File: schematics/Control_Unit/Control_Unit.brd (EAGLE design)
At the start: 49.8 x 49.8 mm, 238 parts, among them IC1 74HCT32N, IC10 74HC74N, IC100 74HCT374N, IC101 74HCT08N, IC102 74HC151N, IC103 74HC373N, IC105 74HC151N, IC106 74HC151N, IC108 74HCT32N, IC11 74HC74N, IC110 74HCT32N, IC111 74HC151N, IC112 74HCT32N, IC113 74HC151N, IC114 74HC151N, IC115 74HC151N, IC116 74HC373N, IC117 74HC74N, IC12 74AC08N, IC124 74HCT32N, IC125 74HCT08N, IC126 74AC157N, IC127 74HCT08N, IC128 74AC08N, IC129 74AC08N, IC13 74AC08N, IC135 74HCT08N, IC136 74HCT08N, IC14 74HC74N, IC141 74HCT32N, IC15 74HC74N, IC16 74AC08N, IC168 74HCT32N, IC169 74HCT32N, IC17 74HCT32N, IC172 74HCT32N, IC173 74HCT32N, IC175 74HC193N, IC176 74HC193N, IC177 74HC193N, IC178 74HC193N, IC179 74HC193N, IC18 74AC08N, IC180 74HC193N, IC181 74HC193N, IC182 74HC193N, IC19 74AC08N, IC190 74HCT32N, IC191 74HCT32N, IC20 74AC08N, IC21 74AC08N, IC22 74HCT32N, IC23 74HCT08N, IC24 74HCT08N, IC26 74HCT08N, IC27 74HCT08N, IC28 74HCT08N, IC29 74HCT32N, IC3 74HC151N, IC30 74HCT08N, IC31 74HCT00N, IC33 74HCT32N, IC34 74HCT08N, IC35 74HCT04N, IC36 74HCT32N, IC38 74HCT08N, IC39 74HCT08N, IC4 74AC08N, IC41 74HCT08N, IC42 74HC373N, IC43 74HCT04N, IC44 74ACT157N, IC46 74ACT157N, IC47 74HCT04N, IC48 74ACT02N, IC49 74AC86N, IC5 74ACT02N, IC51 74HCT08N, IC52 74HCT32N, IC55 74HCT32N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

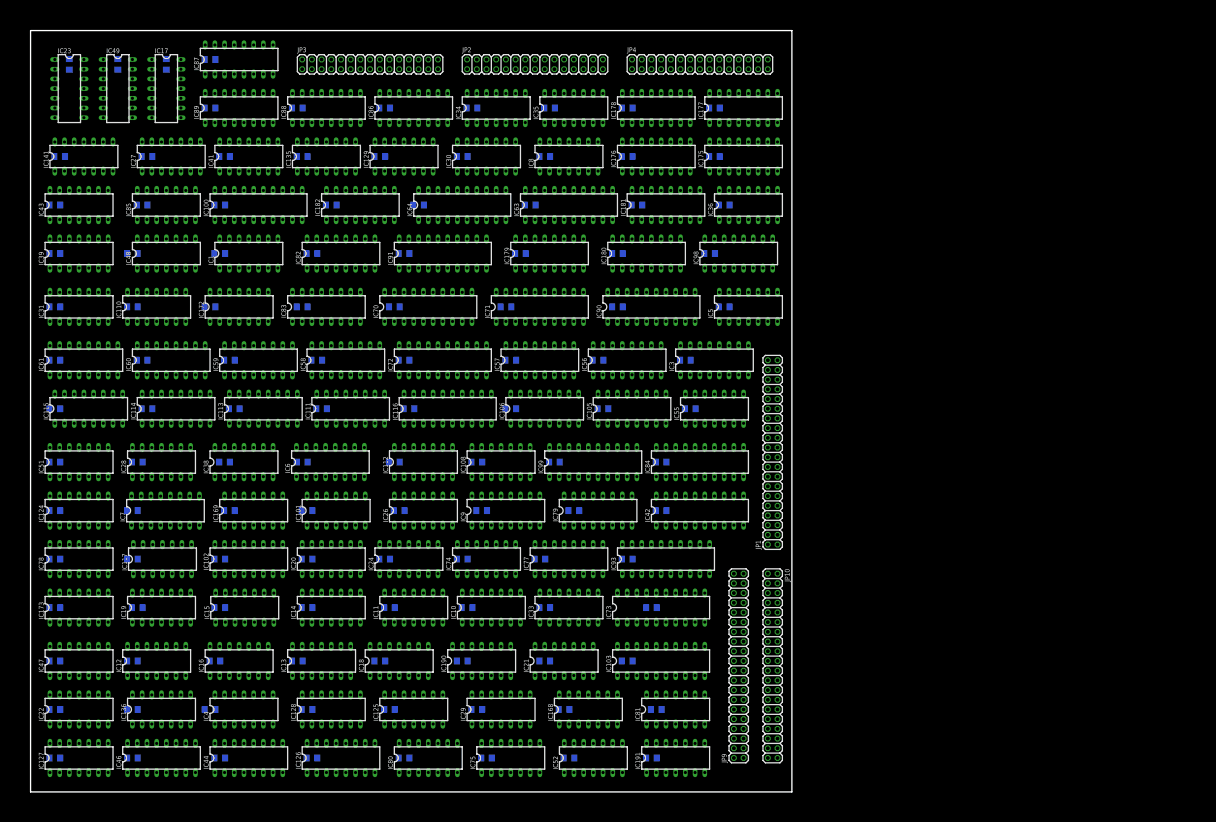
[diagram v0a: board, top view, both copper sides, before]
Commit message: got rid of two cycles! finetuning next
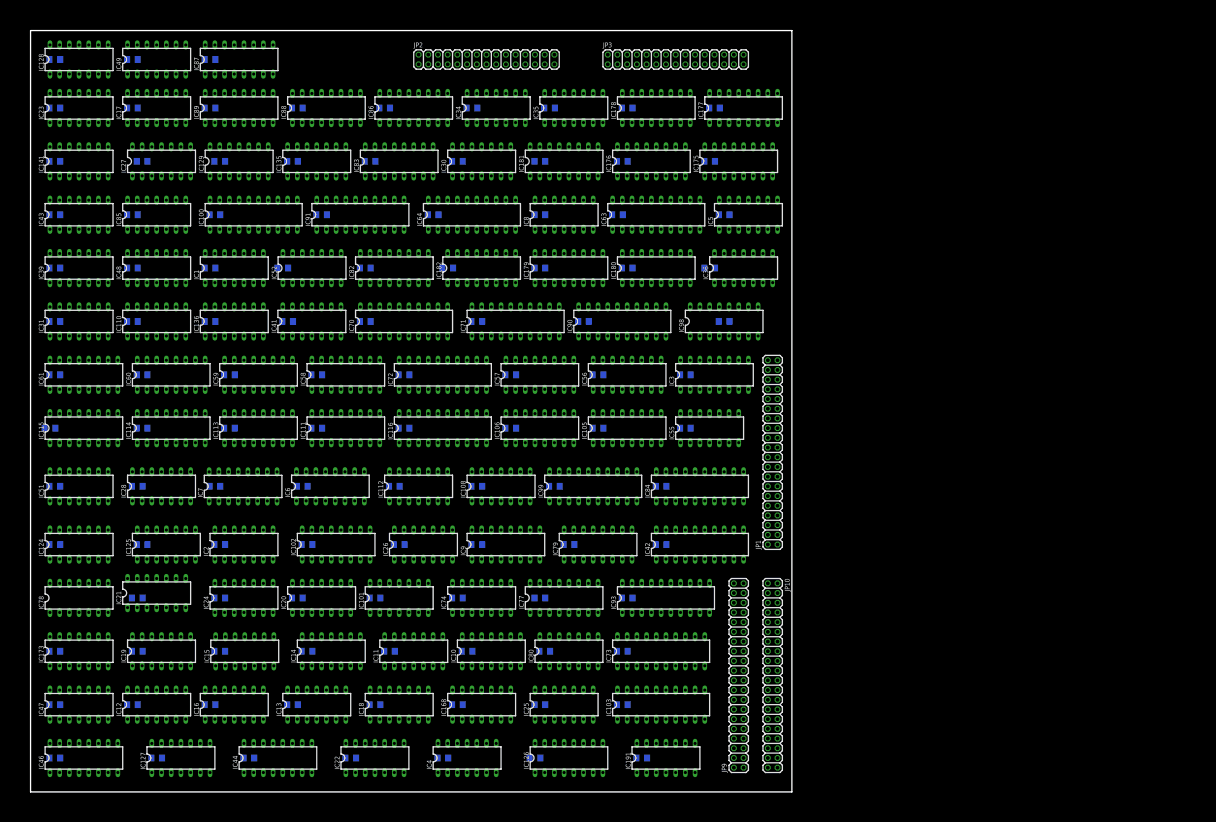
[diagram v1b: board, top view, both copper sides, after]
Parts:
- removed C100, C101, C124, C149, C155, C37, C54, C62: (no value), rcl:C1206
- removed IC117: 74HC74N, 74xx-eu:DIL14
- removed IC169, IC172, IC190, IC29, IC33: 74HCT32N, 74xx-eu:DIL14
- removed IC38, IC75, IC81: 74HCT08N, 74xx-eu:DIL14
- removed JP4: (no value), pinhead:2X15
- added IC2, IC25: 74HCT32N, 74xx-eu:DIL14
- moved C5 48.5 mm to (44.5, 41.3)
- moved C4 48.1 mm to (38.7, 41.3)
- moved IC128 45.6 mm to (3.17, 47.9)
- moved C2 39.4 mm to (1.59, 44.8)
- moved IC52 37.0 mm to (18.4, 34.3)
- moved C74 34.5 mm to (11.7, 34.3)
- moved C145 32.4 mm to (19.1, 37.8)
- moved IC21 27.0 mm to (8.26, 13.0)
- moved IC136 25.8 mm to (13.3, 30.8)
- moved C59 20.1 mm to (42.9, 23.8)
- moved JP3 20.0 mm to (42.2, 47.9)
- moved IC22 19.6 mm to (22.5, 2.22)
- moved IC125 19.5 mm to (8.89, 16.2)
- moved IC4 14.9 mm to (28.6, 2.22)
- moved IC126 14.9 mm to (35.2, 2.22)
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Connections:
- removed net CLR_NOT_CS_LDR: IC17.4, IC173.1, IC173.6
- removed net CLR_NOT_CS_POP: IC172.8, IC48.11, IC85.9
- removed net CONNECT_REG_TO_DBUS_PTR: IC172.11, IC52.4
- removed net FILL_LR_H_SAVE_LR: IC29.9, IC5.11, IC81.3
- removed net FILL_LR_L_SAVE_LR: IC29.1, IC5.8, IC81.8
- removed net FILL_PC_H_RET: IC1.4, IC29.12, IC51.11
- removed net FILL_PC_L_JMP_O: IC1.12, IC101.10, IC33.1, IC38.11
- removed net FILL_PC_L_RET: IC1.13, IC29.4, IC51.3
- removed net FILL_PTR_H_SET_PTR: IC169.1, IC26.8, IC5.3
- removed net FILL_PTR_L_PTR_ADD: IC24.8, IC31.13, IC33.2
- removed net FILL_PTR_L_SET_PTR: IC169.10, IC172.12, IC26.3
- removed net FILL_REGISTER_ALU/ALU_TO_DBUS: IC117.11, IC169.13, IC169.4, IC75.11
- removed net FILL_REGISTER_LDR: IC108.5, IC173.4, IC27.6
- removed net FILL_REGISTER_MOV: IC169.12, IC190.4, IC74.6
- removed net FILL_REGISTER_POP: IC108.4, IC172.9, IC24.6
- removed net IR_LOAD_INPUT: IC127.3, IC80.12, IC90.11
- removed net N$112: IC29.2, IC81.11
- removed net N$122: IC173.5, IC27.3
- removed net N$143: IC168.11, IC168.4
- removed net N$147: IC169.5, IC33.3
- removed net N$155: IC168.12, IC168.3
- removed net N$156: IC172.10, IC24.3
- removed net N$160: IC169.2, IC26.6
- removed net N$18: IC169.6, IC43.9
- removed net N$196: IC172.13, IC24.11
- removed net N$204: IC190.2, IC74.8
- removed net N$223: IC29.5, IC51.6
- removed net N$226: IC29.13, IC51.8
- removed net N$233: IC29.10, IC81.6
- removed net N$56: IC190.5, IC74.3
- removed net PC_COUNT_UP_FETCH2/CYCL_5: IC1.2, IC14.12, IC14.5, JP1.30
- removed net PC_HIGH_LOAD_INPUT_JMP: IC190.9, IC28.11, IC48.5
- removed net PC_LOW_LOAD_INPUT_JMP: IC1.9, IC190.1, IC74.11
- removed net STATE_0/CYCL_6: IC125.1, IC14.9, IC15.2, IC23.12, IC24.12, IC27.9, IC28.1, IC31.9, IC38.9, IC51.4, IC74.1, IC74.9, IC78.12, IC81.12, JP1.32
- removed net STATE_1/CYCL_7: IC15.12, IC15.5, IC23.1, IC23.4, IC24.1, IC26.1, IC27.1, IC27.12, IC38.1, IC51.1, IC74.12, IC74.4, IC75.1, IC81.9, JP1.34
- removed net STATE_2/CYCL_8: IC117.2, IC15.9, IC23.9, IC24.4, IC26.4, IC27.4, IC28.4, IC28.9, IC38.4, IC51.9, IC75.4, IC81.4, JP1.36
- removed net STATE_3/CYCL_9: IC10.2, IC117.5, IC24.9, IC26.9, IC28.12, IC31.1, IC38.12, IC51.12, IC75.12, IC81.1, JP1.38
- removed net WRITE_LR_H_DBUS_RET: IC141.2, IC29.11, IC36.4
- removed net WRITE_LR_L_DBUS_RET: IC141.1, IC29.6
- removed net WRITE_PC_H_DBUS_SAVE_LR: IC141.13, IC29.8
- removed net WRITE_PC_L_DBUS_SAVE_LR: IC141.12, IC29.3, IC36.5
- removed net WRITE_REGB_TO_DBUS_ALU: IC168.9, IC75.6
- removed net WRITE_REGB_TO_DBUS_JMP: IC168.13, IC190.8
- removed net WRITE_REGB_TO_DBUS_JMP_O: IC168.2, IC38.6
- removed net WRITE_REGB_TO_DBUS_PTR_ADD: IC168.1, IC28.6
- removed net WRITE_REGB_TO_DBUS_SET_PTR: IC168.10, IC169.3
- removed net WRITE_REG_TO_DBUS_JMP: IC190.3, IC52.1
- removed net WRITE_REG_TO_DBUS_MOV: IC190.6, IC52.5
- new net CLR_NOT_CS_LDR/FILL_REGISTER_LDR: IC108.5, IC17.4, IC173.1, IC27.8
- new net CLR_NOT_CS_POP/FILL_REGISTER_POP: IC108.4, IC125.3, IC48.11, IC85.9
- new net CONNECT_REG_TO_DBUS_PTR/FILL_PTR_L_SET_PTR: IC24.11, IC48.3, IC52.4
- new net IR_LOAD_INPUT/PC_COUNT_UP_FETCH2: IC1.2, IC127.3, IC80.12, IC90.11
- new net PTR_ADD_OR_JMP_O_OR_ALU_FILL: IC168.4, IC168.8, IC43.9
- new net STATE_0/CYCL_5: IC14.12, IC14.5, IC24.1, IC24.12, IC24.4, IC24.9, IC31.9, IC51.12, IC51.4, IC51.9, IC74.1, IC74.12, IC74.4, IC74.9, JP1.30
- new net STATE_1/CYCL_6: IC125.1, IC14.9, IC15.2, IC23.1, IC26.1, IC26.4, IC27.12, IC27.4, IC27.9, IC28.1, IC28.9, IC51.1, IC78.12, JP1.32
- new net STATE_2/CYCL_7: IC10.2, IC15.5, IC23.4, IC27.1, IC28.12, IC28.4, IC31.1, JP1.34
- new net WRITE_LR_H_DBUS_RET/FILL_PC_H_RET: IC1.4, IC141.2, IC36.4, IC51.3
- new net WRITE_LR_L_DBUS_RET/FILL_PC_L_RET: IC1.13, IC141.1, IC24.3
- new net WRITE_PC_H_DBUS_SAVE_LR/FILL_LR_H_SAVE_LR: IC141.13, IC26.6, IC5.11
- new net WRITE_PC_L_DBUS_SAVE_LR/FILL_LR_L_SAVE_LR: IC141.12, IC24.8, IC36.5, IC5.8
- new net WRITE_REGB_TO_DBUS_ALU/FILL_REGISTER_ALU/ALU_TO_DBUS: IC15.11, IC168.10, IC2.13, IC23.6
- new net WRITE_REGB_TO_DBUS_JMP/PC_HIGH_LOAD_INPUT_JMP: IC168.12, IC28.8, IC5.5
- new net WRITE_REGB_TO_DBUS_JMP_O/FILL_PC_L_JMP_O: IC1.12, IC101.10, IC168.2, IC28.11
- new net WRITE_REGB_TO_DBUS_PTR_ADD/FILL_PTR_L_PTR_ADD: IC168.1, IC28.6, IC31.13
- new net WRITE_REGB_TO_DBUS_SET_PTR/FILL_PTR_H_SET_PTR: IC168.13, IC26.3, IC48.6
- new net WRITE_REG_TO_DBUS_JMP/PC_LOW_LOAD_INPUT_JMP: IC1.9, IC52.1, IC74.8
- new net WRITE_REG_TO_DBUS_MOV/FILL_REGISTER_MOV: IC2.12, IC52.5, IC74.3
- net !CLR_CARRY_BIT: now also IC15.13; no longer IC117.13
- net !OPCODE_5: now also IC26.10; no longer IC75.10
- net !RING_CNTR_RESET: no longer IC117.1, IC15.13
- net !SET_CARRY_BIT: now also IC15.10; no longer IC117.10
- net ADRR_0: no longer JP3.1
- net ADRR_1: no longer JP3.3
- net ADRR_10: no longer JP3.21
- net ADRR_11: no longer JP3.23
- net ADRR_12: no longer JP3.25
- net ADRR_13: no longer JP3.27
- net ADRR_14: no longer JP3.29
- net ADRR_2: no longer JP3.5
- net ADRR_3: no longer JP3.7
- net ADRR_4: no longer JP3.9
- net ADRR_5: no longer JP3.11
- net ADRR_6: no longer JP3.13
- net ADRR_7: no longer JP3.15
- net ADRR_8: no longer JP3.17
- net ADRR_9: no longer JP3.19
- net ALU_CARRY_BIT: now also IC15.9; no longer IC117.9
- net ALU_CARRY_OUT: now also IC15.12; no longer IC117.12
- net ALU_NR1_ENABLE_ALU: now also IC25.9; no longer IC33.9
- net ALU_NR1_ENABLE_JMP_O_PTR_ADD: now also IC25.10; no longer IC33.10
- net ALU_NR2_ENABLE_ALU: now also IC25.12; no longer IC33.4
- net ALU_NR2_ENABLE_JMP_O_PTR_ADD: now also IC25.13; no longer IC33.5
- net CLR_NOT_CS_PUSH: now also IC173.4, IC27.3; no longer IC172.1, IC23.8
- net CLR_NOT_OE/CLR_NOT_CS_CYCL_0: now also IC85.11; no longer IC48.8
- net CLR_NOT_OE_POP: now also JP3.4; no longer JP4.20
- net CONNECT_PTR_TO_ABUS/CLR_NOT_OE_LDR: now also IC85.12; no longer IC48.9
- net CONNECT_PTR_TO_ABUS/CONNECT_REG_TO_DBUS/CLR_NOT_WE/SELECTOR_TABLE_2_STR: now also IC2.9; no longer IC124.1
- net CONNECT_REG_TO_DBUS/CLR_NOT_WE/SELECTOR_TABLE_2_PUSH: now also IC173.6, IC2.10; no longer IC124.2, IC172.3
- net DATA0: no longer JP3.2, JP4.2
- net DATA1: no longer JP3.4, JP4.4
- net DATA2: no longer JP3.6, JP4.6
- net DATA3: no longer JP3.8, JP4.8
- net DATA4: no longer JP3.10, JP4.10
- net DATA5: no longer JP3.12, JP4.12
- net DATA6: no longer JP3.14, JP4.14
- net DATA7: no longer JP3.16, JP4.16
- net DBUS_SELECTOR_TABLE_2: now also IC2.8; no longer IC124.3
- net GND: now also IC2.7, IC25.7, JP1.36, JP1.38, JP3.10, JP3.14, JP3.2; no longer C100.2, C101.2, C124.2, C149.2, C155.2, C37.2, C54.2, C62.2, IC117.7, IC169.7, IC172.7, IC190.7, IC29.7, IC33.7, IC38.7, IC75.7, IC81.7, JP4.18, JP4.26, JP4.30
- net HGGJHGGJZGZ77UZGHGHHGHGHGHGHJGHJ: now also IC51.8; no longer IC28.3
- net INPUT_REG_IS_NOT_OUTPUT_REG: now also IC108.9, IC2.6; no longer IC108.8, IC5.5
- net LATCH_ALU_INPUT_B_ALU: now also IC124.1, IC28.3; no longer IC190.12, IC75.3
- net LATCH_ALU_INPUT_B_JMP_O: now also IC78.11, IC80.1; no longer IC172.4, IC38.3
- net LDR: now also IC27.10, IC51.10; no longer IC27.2, IC27.5, IC28.2
- net MEM_NOT_OE: now also IC85.13; no longer IC48.10
- net N$109: now also IC74.11, IC80.2; no longer IC172.5, IC38.8
- net N$11: now also IC168.3, IC168.9; no longer IC169.8, IC43.11
- net N$110: now also IC124.2, IC74.6; no longer IC190.13, IC78.11
- net N$123: now also IC51.11; no longer IC27.8
- net N$132: now also IC28.13, IC74.13, IC78.13; no longer IC38.10, IC38.13, IC38.2, IC38.5
- net N$146: now also IC173.5, IC27.6; no longer IC172.2, IC23.6
- net N$148: now also IC25.11; no longer IC33.6
- net N$15: no longer IC28.13, IC74.13
- net N$151: now also IC24.6; no longer IC125.3
- net N$157: now also IC51.6; no longer IC23.11
- net N$163: now also IC5.3; no longer IC48.3
- net N$193: now also IC48.8; no longer IC85.11
- net N$194: now also IC24.10, IC26.5; no longer IC81.10, IC81.13, IC81.2, IC81.5
- net N$20: now also IC48.9; no longer IC85.12
- net N$202: now also IC25.8; no longer IC33.8
- net N$219: now also IC24.2, IC26.8; no longer IC51.10, IC51.13, IC51.5, IC75.8
- net N$236: now also JP3.8; no longer JP4.24
- net N$237: now also JP3.6; no longer JP4.22
- net N$32: now also IC5.2; no longer IC48.2
- net N$33: now also IC5.6; no longer IC48.6
- net N$4: now also IC168.11; no longer IC168.8
- net N$45: now also IC108.10; no longer IC5.6
- net N$47: now also IC2.3; no longer IC33.11
- net N$48: now also IC2.4; no longer IC108.9
- net N$5: now also IC108.8, IC43.11; no longer IC190.10, IC28.8
- net N$51: now also IC2.5; no longer IC108.10
- net N$55: no longer IC74.5
- net N$6: now also IC2.11; no longer IC169.11
- net N$97: no longer IC26.10, IC26.5
- net PC_HIGH_LOAD_INPUT_NOT: now also IC5.4; no longer IC48.4
- net PC_LOW_LOAD_INPUT_NOT: now also IC5.1; no longer IC48.1
- net POP: now also IC125.2, IC51.5; no longer IC23.13, IC24.2, IC24.5
- net PTR_ADD: now also IC24.5; no longer IC125.2, IC24.10
- net PTR_H_LOAD_INPUT_NOT: now also IC48.4; no longer IC5.1
- net PTR_L_LOAD_INPUT_NOT: now also IC48.1; no longer IC43.10
- net PUSH: now also IC27.2, IC27.5; no longer IC23.10, IC23.5
- net REG0_ZERO: now also IC48.10; no longer IC85.13
- net RING_CNTR_CLOCK: no longer IC117.3, IC15.11
- net SAVE_LR/RET: now also IC26.9; no longer IC75.9
- net SECOND_LATCH_SELECT: now also IC2.1; no longer IC33.12
- net SELECT_CARRY_BIT: now also IC23.5, IC28.2, IC74.5; no longer IC75.13, IC75.2, IC75.5, IC78.13
- net SP_DATA_OUT_0: now also JP3.1; no longer JP4.1
- net SP_DATA_OUT_1: now also JP3.3; no longer JP4.3
- net SP_DATA_OUT_10: now also JP3.21; no longer JP4.21
- net SP_DATA_OUT_11: now also JP3.23; no longer JP4.23
- net SP_DATA_OUT_12: now also JP3.25; no longer JP4.25
- net SP_DATA_OUT_13: now also JP3.27; no longer JP4.27
- net SP_DATA_OUT_14: now also JP3.29; no longer JP4.29
- net SP_DATA_OUT_2: now also JP3.5; no longer JP4.5
- net SP_DATA_OUT_3: now also JP3.7; no longer JP4.7
- net SP_DATA_OUT_4: now also JP3.9; no longer JP4.9
- net SP_DATA_OUT_5: now also JP3.11; no longer JP4.11
- net SP_DATA_OUT_6: now also JP3.13; no longer JP4.13
- net SP_DATA_OUT_7: now also JP3.15; no longer JP4.15
- net SP_DATA_OUT_8: now also JP3.17; no longer JP4.17
- net SP_DATA_OUT_9: now also JP3.19; no longer JP4.19
- net STR: now also IC51.13; no longer IC27.10
- net TABLE_1_INPUT_PTR_HIGH: now also IC48.5; no longer IC5.2
- net TABLE_1_INPUT_PTR_L: now also IC48.2; no longer IC169.9
- net TWO_BYTE_CMD: now also IC43.10; no longer IC5.4
- net VCC: now also IC2.14, IC25.14, JP3.12; no longer C100.1, C101.1, C124.1, C149.1, C155.1, C37.1, C54.1, C62.1, IC117.14, IC117.4, IC15.10, IC169.14, IC172.14, IC190.14, IC29.14, IC33.14, IC38.14, IC75.14, IC81.14, JP4.28
- net WRITE_PC_L_ALU_LATCH_JMP_O: now also IC80.3; no longer IC172.6
- net WRITE_PTR_L_TO_DBUS_PTR_ADD: now also IC2.2; no longer IC33.13
- net WRITE_REG_TO_DBUS_ALU: now also IC124.3; no longer IC190.11

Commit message: clean up docs and schematic. no functional changes
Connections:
- net CONNECT_PTR_TO_ABUS/CONNECT_REG_TO_DBUS/CLR_NOT_WE/SELECTOR_TABLE_2_STR renamed CNNCT_PTR_TO_ABUS/CNNCT_REG_TO_DBUS/CLR_NOT_WE/SELECTOR_2_STR
- net INPUT_REG0/OPCODE_5/OPCODE_4_IS_NULL renamed INPUT_REG0/OPC4/5_IS_NULL
- net UNUSED renamed NOT_USED1
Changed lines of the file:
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@@
 <contactref element="IC85" pad="14"/>
 <contactref element="JP2" pad="28"/>
-<contactref element="JP3" pad="28"/>
 <contactref element="C14" pad="1"/>
 <contactref element="C32" pad="1"/>
@@
 <contactref element="IC6" pad="16"/>
 <contactref element="IC7" pad="16"/>
-<contactref element="IC7" pad="11"/>
-<contactref element="IC6" pad="11"/>
-<contactref element="IC6" pad="4"/>
 <contactref element="IC180" pad="4"/>
-<contactref element="IC7" pad="4"/>
 <contactref element="IC5" pad="14"/>
 <contactref element="IC8" pad="14"/>
@@
 <contactref element="IC2" pad="14"/>
 <contactref element="IC25" pad="14"/>
+<contactref element="IC7" pad="11"/>
+<contactref element="IC6" pad="11"/>
+<contactref element="IC6" pad="4"/>
+<contactref element="IC7" pad="4"/>
+<contactref element="JP3" pad="28"/>
 <wire x1="47.625" y1="45.72" x2="46.0375" y2="48.26" width="0" layer="19" extent="1-1"/>
 <wire x1="44.45" y1="45.72" x2="46.0375" y2="48.26" width="0" layer="19" extent="1-1"/>
@@
 <wire x1="9.8425" y1="1.27" x2="4.445" y2="1.27" width="0" layer="19" extent="1-1"/>
 </signal>
-<signal name="INPUT_REG0/OPCODE_5/OPCODE_4_IS_NULL">
+<signal name="INPUT_REG0/OPC4/5_IS_NULL">
 <contactref element="IC129" pad="3"/>
 <contactref element="IC30" pad="1"/>
@@
 <wire x1="2.54" y1="8.255" x2="7.62" y2="38.735" width="0" layer="19" extent="1-1"/>
 </signal>
-<signal name="CONNECT_PTR_TO_ABUS/CONNECT_REG_TO_DBUS/CLR_NOT_WE/SELECTOR_TABLE_2_STR">
+<signal name="CNNCT_PTR_TO_ABUS/CNNCT_REG_TO_DBUS/CLR_NOT_WE/SELECTOR_2_STR">
 <contactref element="IC173" pad="8"/>
 <contactref element="IC35" pad="3"/>
@@
 <wire x1="19.945" y1="19.0525" x2="48.895" y2="16.8275" width="0" layer="19" extent="1-1"/>
 </signal>
-<signal name="UNUSED">
+<signal name="NOT_USED1">
 <contactref element="IC34" pad="6"/>
 </signal>

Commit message: finished COntrolUnit. Not much left to do
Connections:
- net CNNCT_PTR_TO_ABUS/CNNCT_REG_TO_DBUS/CLR_NOT_WE/SELECTOR_2_STR renamed CNNCT_PTR_TO_ABUS/CNNCT_REG_TO_DBUS/CLR_NOT_WE/SEL_2_STR
- net WRITE_LR_H_DBUS_RET/FILL_PC_H_RET renamed WRITE_LR_H_DBUS/FILL_PC_H_RET
- net WRITE_PC_L_DBUS_SAVE_LR/FILL_LR_L_SAVE_LR renamed WRITE_PC_L_DBUS/FILL_LR_L_SAVE_LR
- net WRITE_REGB_TO_DBUS_ALU/FILL_REGISTER_ALU/ALU_TO_DBUS renamed WRITE_REGB_TO_DBUS/FILL_REGISTER/ALU_TO_DBUS_ALU
- net WRITE_REGB_TO_DBUS_JMP_O/FILL_PC_L_JMP_O renamed WRITE_REGB_TO_DBUS/FILL_PC_L_JMP_O
- net WRITE_REGB_TO_DBUS_PTR_ADD/FILL_PTR_L_PTR_ADD renamed WRITE_REGB_TO_DBUS/FILL_PTR_L_PTR_ADD
- removed net CYCL_3: IC11.12, IC11.5, IC127.13, JP1.26
- removed net CYCL_4: IC11.9, IC127.1, IC14.2, JP1.28
- removed net IR_LOAD_INPUT/PC_COUNT_UP_FETCH2: IC1.2, IC127.3, IC80.12, IC90.11
- removed net NOT_USED1: IC34.6
- removed net PC_COUNT_UP_FETCH1: IC1.1, IC127.11, IC80.13
- new net !TWO_BYTE_CMD: IC108.8, IC23.10, IC43.11
- new net IR_LOAD_INPUT/PC_COUNT_UP_FETCH2/CYCL_4: IC1.2, IC11.9, IC25.1, IC80.12, IC90.11, JP1.28
- new net N$44: IC11.5, IC23.12, IC23.9
- new net N$56: IC14.2, IC25.3
- new net PC_COUNT_UP_FETCH1/CYCL_3: IC1.1, IC11.12, IC23.11, IC80.13, JP1.26
- net !IR_DATA_OUT_7: now also IC127.10; no longer IC127.9
- net ALU_CARRY_BIT: now also IC34.4; no longer IC34.12
- net ALU_CARRY_IN: now also IC34.6; no longer IC34.11
- net DATA_BUS_ENABLE_LATCH: now also IC127.3; no longer IC34.3
- net GND: now also JP9.36, JP9.38
- net INPUT_REG2: no longer IC34.4
- net N$12: now also IC127.11; no longer IC34.8
- net N$132: now also IC124.4; no longer IC124.5
- net N$166: now also IC127.9; no longer IC127.10
- net N$239: no longer IC34.5
- net N$266: now also IC127.13, IC127.2; no longer IC34.10, IC34.2
- net N$5: now also IC23.8, IC25.2; no longer IC108.8, IC43.11
- net N$7: now also IC127.1; no longer IC34.1
- net PC_L_LOAD_INPUT_TABLE_1: now also IC1.13; no longer IC1.10
- net PTR_ADD: now also IC124.5; no longer IC124.4
- net REGISTER_OUTPUT_SEL_3: now also IC127.12; no longer IC34.9
- net SELECT_CARRY_BIT: now also IC34.5; no longer IC34.13
- net TWO_BYTE_CMD: now also IC23.13; no longer IC127.12, IC127.2
- net WRITE_LR_L_DBUS_RET/FILL_PC_L_RET: now also IC1.10; no longer IC1.13

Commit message: improve layout
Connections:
- net CLR_NOT_CS_LDR/FILL_REGISTER_LDR renamed CLR_NOT_CS/FILL_REGISTER_LDR
- net WRITE_PC_H_DBUS_SAVE_LR/FILL_LR_H_SAVE_LR renamed WRITE_PC_H_DBUS/FILL_LR_H_SAVE_LR
- net WRITE_REGB_TO_DBUS_SET_PTR/FILL_PTR_H_SET_PTR renamed WRITE_REGB_TO_DBUS/FILL_PTR_H_SET_PTR
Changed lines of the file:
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@@
 <wire x1="1.905" y1="8.255" x2="5.08" y2="20.955" width="0" layer="19" extent="1-1"/>
 </signal>
-<signal name="CLR_NOT_CS_LDR/FILL_REGISTER_LDR">
+<signal name="CLR_NOT_CS/FILL_REGISTER_LDR">
 <contactref element="IC173" pad="1"/>
 <contactref element="IC17" pad="4"/>
@@
 <wire x1="11.43" y1="46.99" x2="11.43" y2="43.815" width="0" layer="19" extent="1-1"/>
 </signal>
-<signal name="WRITE_REGB_TO_DBUS_SET_PTR/FILL_PTR_H_SET_PTR">
+<signal name="WRITE_REGB_TO_DBUS/FILL_PTR_H_SET_PTR">
 <contactref element="IC26" pad="3"/>
 <contactref element="IC48" pad="6"/>
@@
 <wire x1="13.335" y1="11.7475" x2="13.97" y2="35.2425" width="0" layer="19" extent="1-1"/>
 </signal>
-<signal name="WRITE_PC_H_DBUS_SAVE_LR/FILL_LR_H_SAVE_LR">
+<signal name="WRITE_PC_H_DBUS/FILL_LR_H_SAVE_LR">
 <contactref element="IC141" pad="13"/>
 <contactref element="IC5" pad="11"/>

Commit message: fix latex docs
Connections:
- net CLR_NOT_OE/CLR_NOT_CS_CYCL_0 renamed CLR_NOT_OE/CLR_NOT_CS_CYCL_1/2
- net CLR_NOT_OE/CLR_NOT_CS_CYCL_2 renamed CLR_NOT_OE/CLR_NOT_CS_CYCL_3/4
- net WRITE_REGB_TO_DBUS_JMP/PC_HIGH_LOAD_INPUT_JMP renamed WRITE_REGB_TO_DBUS/PC_HIGH_LOAD_INPUT_JMP
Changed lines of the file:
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@@
 <?xml version="1.0" encoding="utf-8"?>
 <!DOCTYPE eagle SYSTEM "eagle.dtd">
-<eagle version="6.2">
+<eagle version="6.5.0">
 <drawing>
 <settings>
@@
 <wire x1="49.835" y1="49.8375" x2="0" y2="49.8375" width="0" layer="20"/>
 <wire x1="0" y1="49.8375" x2="0" y2="0" width="0" layer="20"/>
-<dimension x1="0" y1="49.8375" x2="49.8475" y2="50.165" x3="24.907090625" y3="52.53696875" layer="16"/>
-<dimension x1="49.835" y1="49.8375" x2="49.8475" y2="0" x3="62.859225" y3="24.9220125" layer="16"/>
+<dimension x1="0" y1="49.8375" x2="49.8475" y2="50.165" x3="24.907090625" y3="52.53696875" textsize="3.5" layer="16"/>
+<dimension x1="49.835" y1="49.8375" x2="49.8475" y2="0" x3="62.859225" y3="24.9220125" textsize="3.5" layer="16"/>
 </plain>
 <attributes>
@@
 </class>
 </classes>
-<designrules>
+<designrules name="default">
 <description language="de">&lt;b&gt;EAGLE Design Rules&lt;/b&gt;
 &lt;p&gt;
@@
 <wire x1="48.895" y1="7.9375" x2="48.26" y2="7.9375" width="0" layer="19" extent="1-1"/>
 </signal>
-<signal name="CLR_NOT_OE/CLR_NOT_CS_CYCL_0">
+<signal name="CLR_NOT_OE/CLR_NOT_CS_CYCL_1/2">
 <contactref element="IC17" pad="1"/>
 <contactref element="IC80" pad="6"/>
@@
 <wire x1="3.175" y1="3.175" x2="1.27" y2="36.83" width="0" layer="19" extent="1-1"/>
 </signal>
-<signal name="WRITE_REGB_TO_DBUS_JMP/PC_HIGH_LOAD_INPUT_JMP">
+<signal name="WRITE_REGB_TO_DBUS/PC_HIGH_LOAD_INPUT_JMP">
 <contactref element="IC28" pad="8"/>
 <contactref element="IC5" pad="5"/>
@@
 <wire x1="3.81" y1="38.735" x2="1.905" y2="45.72" width="0" layer="19" extent="1-1"/>
 </signal>
-<signal name="CLR_NOT_OE/CLR_NOT_CS_CYCL_2">
+<signal name="CLR_NOT_OE/CLR_NOT_CS_CYCL_3/4">
 <contactref element="IC80" pad="11"/>
 <contactref element="IC17" pad="5"/>
